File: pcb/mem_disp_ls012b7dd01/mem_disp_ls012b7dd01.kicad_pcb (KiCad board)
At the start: 2 copper layers, 11 x 41.5 mm, 4 parts, among them J1 Pin Header, J2 FCP Connector

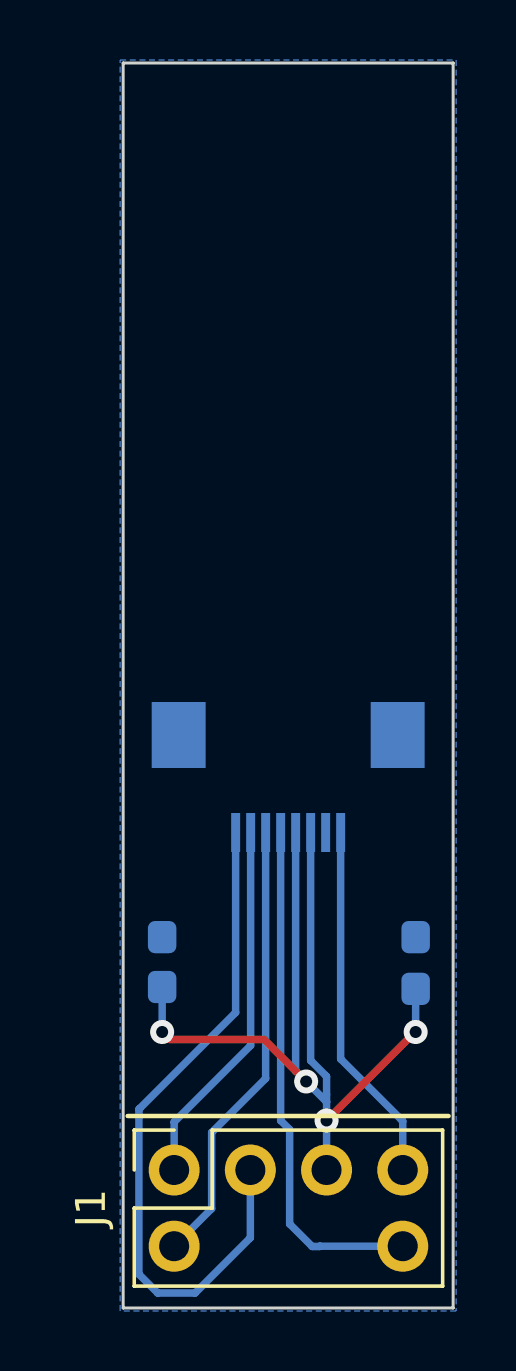
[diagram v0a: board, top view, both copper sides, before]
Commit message: Fixed capacitor mix up
VDD pin was connected to DISP capacitor and DISP capacitor was connected to VDD.

From an electrical perspective it didn’t matter though.
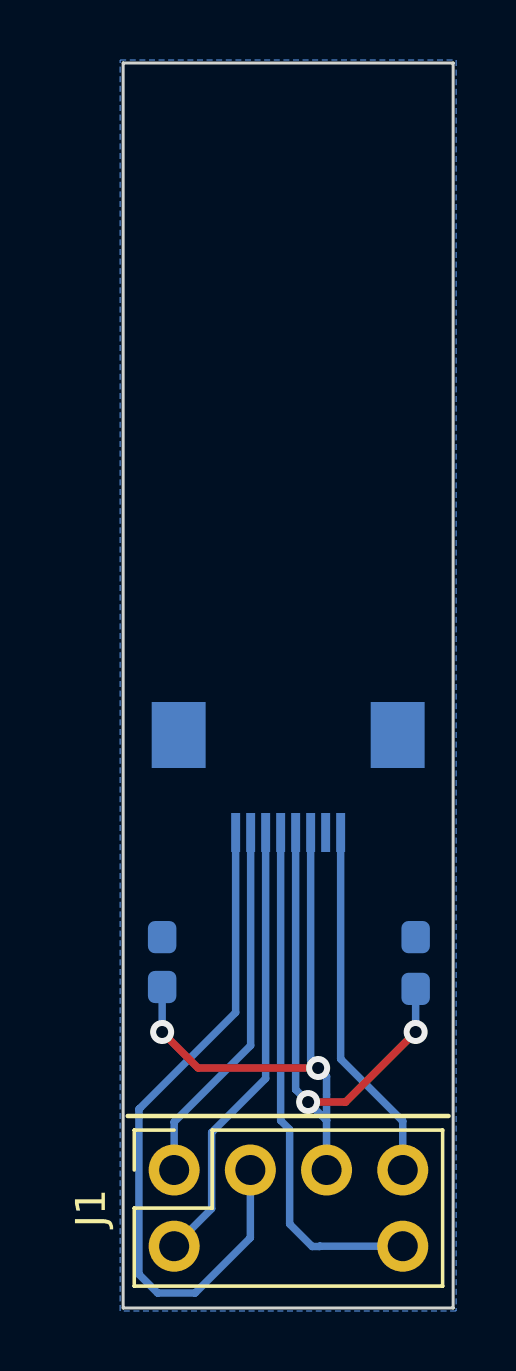
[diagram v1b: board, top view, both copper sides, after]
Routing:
- net VDD: track 33.5 -> 34.7 mm
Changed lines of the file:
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@@
     (style (thickness 0.15) (arrow_length 1.27) (text_position_mode 0) (extension_height 0.58642) (extension_offset 0.5) keep_text_aligned)
   )
-  (segment (start 51.55 83.05) (end 54.7 83.05) (width 0.25) (layer "F.Cu") (net 1))
-  (segment (start 51.3 82.8) (end 51.55 83.05) (width 0.25) (layer "F.Cu") (net 1))
-  (segment (start 54.7 83.05) (end 56.1 84.45) (width 0.25) (layer "F.Cu") (net 1))
-  (segment (start 56.78 85.75) (end 59.73 82.8) (width 0.25) (layer "F.Cu") (net 1))
-  (segment (start 59.73 82.8) (end 59.75 82.8) (width 0.25) (layer "F.Cu") (net 1))
+  (segment (start 56.165 85.135) (end 57.415 85.135) (width 0.25) (layer "F.Cu") (net 1))
+  (segment (start 52.5 84) (end 51.3 82.8) (width 0.25) (layer "F.Cu") (net 1))
+  (segment (start 57.415 85.135) (end 59.75 82.8) (width 0.25) (layer "F.Cu") (net 1))
+  (segment (start 56.5 84) (end 52.5 84) (width 0.25) (layer "F.Cu") (net 1))
+  (via (at 56.165 85.135) (size 0.8) (drill 0.4) (layers "F.Cu" "B.Cu") (net 1))
+  (via (at 51.3 82.8) (size 0.8) (drill 0.4) (layers "F.Cu" "B.Cu") (net 1))
   (via (at 59.75 82.8) (size 0.8) (drill 0.4) (layers "F.Cu" "B.Cu") (net 1))
-  (via (at 56.1 84.45) (size 0.8) (drill 0.4) (layers "F.Cu" "B.Cu") (net 1))
-  (via (at 51.3 82.8) (size 0.8) (drill 0.4) (layers "F.Cu" "B.Cu") (net 1))
-  (via (at 56.78 85.75) (size 0.8) (drill 0.4) (layers "F.Cu" "B.Cu") (net 1))
-  (segment (start 55.75 76.15) (end 55.75 84.1) (width 0.25) (layer "B.Cu") (net 1))
+  (via (at 56.5 84) (size 0.8) (drill 0.4) (layers "F.Cu" "B.Cu") (net 1))
   (segment (start 56.78 84.88) (end 56.78 84.28) (width 0.25) (layer "B.Cu") (net 1))
   (segment (start 56.78 85.75) (end 56.78 85.13) (width 0.25) (layer "B.Cu") (net 1))
-  (segment (start 55.75 84.1) (end 56.1 84.45) (width 0.25) (layer "B.Cu") (net 1))
   (segment (start 51.3 82.8) (end 51.3 81.3) (width 0.25) (layer "B.Cu") (net 1))
-  (segment (start 56.78 84.28) (end 56.25 83.75) (width 0.25) (layer "B.Cu") (net 1))
-  (segment (start 56.1 84.45) (end 56.78 85.13) (width 0.25) (layer "B.Cu") (net 1))
+  (segment (start 55.75 76.15) (end 55.75 84.72) (width 0.25) (layer "B.Cu") (net 1))
+  (segment (start 55.75 84.72) (end 56.165 85.135) (width 0.25) (layer "B.Cu") (net 1))
+  (segment (start 56.78 84.28) (end 56.5 84) (width 0.25) (layer "B.Cu") (net 1))
+  (segment (start 56.165 85.135) (end 56.78 85.75) (width 0.25) (layer "B.Cu") (net 1))
   (segment (start 56.78 85.75) (end 56.78 87.4) (width 0.25) (layer "B.Cu") (net 1))
   (segment (start 56.25 83.75) (end 56.25 76.15) (width 0.25) (layer "B.Cu") (net 1))
   (segment (start 59.75 82.8) (end 59.75 81.3625) (width 0.25) (layer "B.Cu") (net 1))
+  (segment (start 56.5 84) (end 56.25 83.75) (width 0.25) (layer "B.Cu") (net 1))
   (segment (start 56.78 85.13) (end 56.78 84.88) (width 0.25) (layer "B.Cu") (net 1))
   (segment (start 59.32 85.77) (end 59.275 85.725) (width 0.25) (layer "B.Cu") (net 2))

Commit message: Fixed C1 capacity from 20uF to 2.0uF
The 2017 datasheet seems to show that a 20uF capacitor is requiered, but in reality 2.0uF is the correct value.

The font in the datasheet is squished, which causes the "." to merge with the
"2".

Older datasheets also show a value of 2.0.
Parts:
- C2: value 20uF -> 2.0uF
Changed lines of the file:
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@@
       (effects (font (size 1 1) (thickness 0.15)) (justify mirror))
     )
-    (fp_text value "20uF" (at 0 -1.43 90) (layer "B.Fab") hide
+    (fp_text value "2.0uF" (at 0 -1.43 90) (layer "B.Fab") hide
       (effects (font (size 1 1) (thickness 0.15)) (justify mirror))
     )

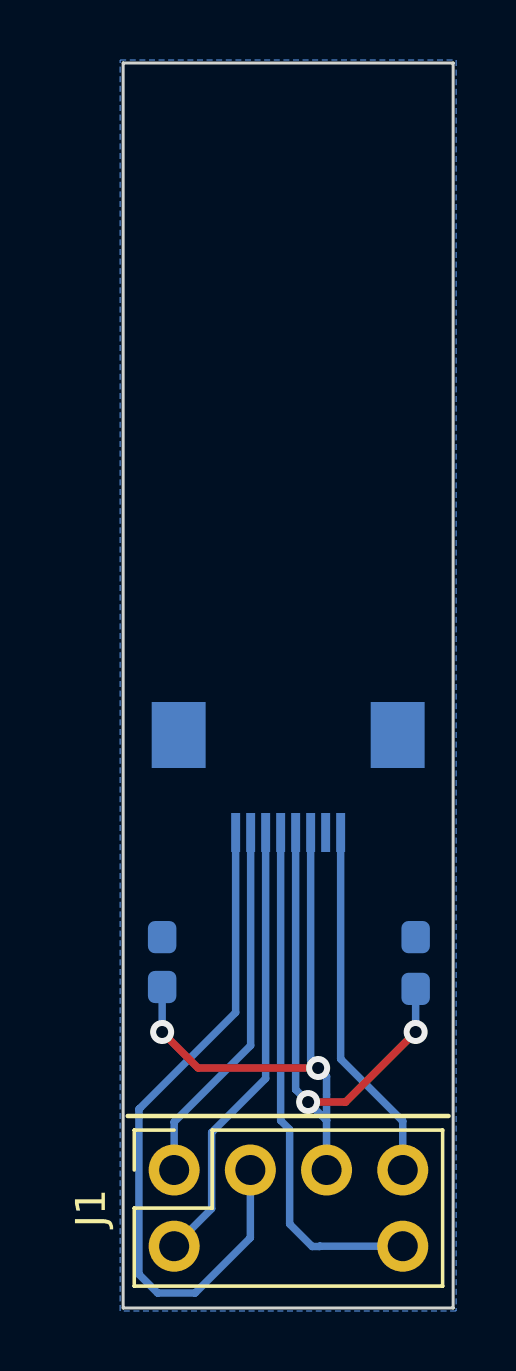
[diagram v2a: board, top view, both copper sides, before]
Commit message: Removed DISP C1 capacitor
The datasheet calls for a 560pF capacitor (C1) connected to DISP, but since we are connecting DISP to VDD, which already has a large capacitor, that's not necessary.
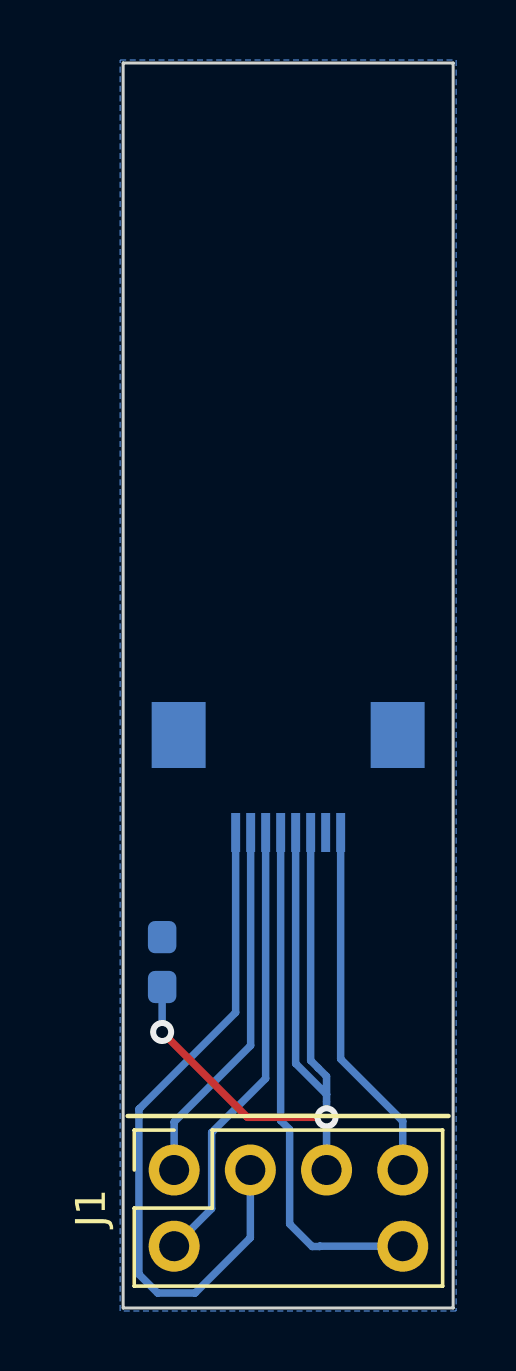
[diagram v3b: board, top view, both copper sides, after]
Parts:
- removed C1: 560pF/680pF, Capacitor_SMD:C_0603_1608Metric_Pad1.08x0.95mm_HandSolder
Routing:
- net VDD: track 34.7 -> 28.8 mm, vias 4 -> 2
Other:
- board text added: "Shap Memory Disp. (LS012B7DD01) Breakout Board v0.2"
- board text removed: "Shap Memory Disp. (LS012B7DD01) Breakout Board v0.1"
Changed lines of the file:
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@@
-    )
-  )
-  (footprint "Capacitor_SMD:C_0603_1608Metric_Pad1.08x0.95mm_HandSolder" (layer "B.Cu")
-    (at 59.75 80.5 90)
-    (descr "Capacitor SMD 0603 (1608 Metric), square (rectangular) end terminal, IPC_7351 nominal with elongated pad for handsoldering. (Body size source: IPC-SM-782 page 76, https://www.pcb-3d.com/wordpress/wp-content/uploads/ipc-sm-782a_amendment_1_and_2.pdf), generated with kicad-footprint-generator")
-    (tags "capacitor handsolder")
-    (property "Sheetfile" "mem_disp_ls012b7dd01.kicad_sch")
-    (property "Sheetname" "")
-    (attr smd)
-    (fp_text reference "C1" (at 2.35 0 180) (layer "B.SilkS")
-      (effects (font (size 1 1) (thickness 0.15)) (justify mirror))
-    )
-    (fp_text value "560pF/680pF" (at -2.85 3.1 90) (layer "B.Fab") hide
-      (effects (font (size 1 1) (thickness 0.15)) (justify mirror))
-    )
-    (fp_text user "${REFERENCE}" (at 0 0 90) (layer "B.Fab")
-      (effects (font (size 0.4 0.4) (thickness 0.06)) (justify mirror))
-    )
-    (fp_line (start -0.146267 0.51) (end 0.146267 0.51) (layer "B.SilkS") (width 0.12))
-    (fp_line (start -0.146267 -0.51) (end 0.146267 -0.51) (layer "B.SilkS") (width 0.12))
-    (fp_line (start -1.65 0.73) (end 1.65 0.73) (layer "B.CrtYd") (width 0.05))
-    (fp_line (start 1.65 0.73) (end 1.65 -0.73) (layer "B.CrtYd") (width 0.05))
-    (fp_line (start -1.65 -0.73) (end -1.65 0.73) (layer "B.CrtYd") (width 0.05))
-    (fp_line (start 1.65 -0.73) (end -1.65 -0.73) (layer "B.CrtYd") (width 0.05))
-    (fp_line (start 0.8 0.4) (end 0.8 -0.4) (layer "B.Fab") (width 0.1))
-    (fp_line (start -0.8 -0.4) (end -0.8 0.4) (layer "B.Fab") (width 0.1))
-    (fp_line (start 0.8 -0.4) (end -0.8 -0.4) (layer "B.Fab") (width 0.1))
-    (fp_line (start -0.8 0.4) (end 0.8 0.4) (layer "B.Fab") (width 0.1))
-    (pad "1" smd roundrect (at -0.8625 0 90) (size 1.075 0.95) (layers "B.Cu" "B.Paste" "B.Mask") (roundrect_rratio 0.25)
-      (net 1 "VDD") (pintype "passive"))
-    (pad "2" smd roundrect (at 0.8625 0 90) (size 1.075 0.95) (layers "B.Cu" "B.Paste" "B.Mask") (roundrect_rratio 0.25)
-      (net 2 "GND") (pintype "passive"))
-    (model "${KICAD6_3DMODEL_DIR}/Capacitor_SMD.3dshapes/C_0603_1608Metric.wrl"
-      (offset (xyz 0 0 0))
-      (scale (xyz 1 1 1))
-      (rotate (xyz 0 0 0))
     )
   )
@@
   (gr_line (start 61 92) (end 61 50.5) (layer "Edge.Cuts") (width 0.1))
   (gr_line (start 50 92) (end 61 92) (layer "Edge.Cuts") (width 0.1))
-  (gr_text "Shap Memory Disp.\n(LS012B7DD01)\nBreakout Board v0.1" (at 55.6 53.4) (layer "B.SilkS")
+  (gr_text "Shap Memory Disp.\n(LS012B7DD01)\nBreakout Board v0.2" (at 55.6 53.4) (layer "B.SilkS")
     (effects (font (size 0.5 0.5) (thickness 0.125)) (justify mirror))
   )
@@
     (style (thickness 0.15) (arrow_length 1.27) (text_position_mode 0) (extension_height 0.58642) (extension_offset 0.5) keep_text_aligned)
   )
-  (segment (start 56.165 85.135) (end 57.415 85.135) (width 0.25) (layer "F.Cu") (net 1))
-  (segment (start 52.5 84) (end 51.3 82.8) (width 0.25) (layer "F.Cu") (net 1))
-  (segment (start 57.415 85.135) (end 59.75 82.8) (width 0.25) (layer "F.Cu") (net 1))
-  (segment (start 56.5 84) (end 52.5 84) (width 0.25) (layer "F.Cu") (net 1))
-  (via (at 56.165 85.135) (size 0.8) (drill 0.4) (layers "F.Cu" "B.Cu") (net 1))
+  (segment (start 54.145 85.645) (end 51.3 82.8) (width 0.25) (layer "F.Cu") (net 1))
+  (segment (start 56.78 85.645) (end 54.145 85.645) (width 0.25) (layer "F.Cu") (net 1))
   (via (at 51.3 82.8) (size 0.8) (drill 0.4) (layers "F.Cu" "B.Cu") (net 1))
-  (via (at 59.75 82.8) (size 0.8) (drill 0.4) (layers "F.Cu" "B.Cu") (net 1))
-  (via (at 56.5 84) (size 0.8) (drill 0.4) (layers "F.Cu" "B.Cu") (net 1))
+  (via (at 56.78 85.645) (size 0.8) (drill 0.4) (layers "F.Cu" "B.Cu") (net 1))
+  (segment (start 56.78 85.645) (end 56.78 85.13) (width 0.25) (layer "B.Cu") (net 1))
+  (segment (start 55.75 83.85) (end 56.78 84.88) (width 0.25) (layer "B.Cu") (net 1))
   (segment (start 56.78 84.88) (end 56.78 84.28) (width 0.25) (layer "B.Cu") (net 1))
-  (segment (start 56.78 85.75) (end 56.78 85.13) (width 0.25) (layer "B.Cu") (net 1))
+  (segment (start 56.78 85.75) (end 56.78 85.645) (width 0.25) (layer "B.Cu") (net 1))
   (segment (start 51.3 82.8) (end 51.3 81.3) (width 0.25) (layer "B.Cu") (net 1))
-  (segment (start 55.75 76.15) (end 55.75 84.72) (width 0.25) (layer "B.Cu") (net 1))
-  (segment (start 55.75 84.72) (end 56.165 85.135) (width 0.25) (layer "B.Cu") (net 1))
+  (segment (start 55.75 76.15) (end 55.75 83.85) (width 0.25) (layer "B.Cu") (net 1))
   (segment (start 56.78 84.28) (end 56.5 84) (width 0.25) (layer "B.Cu") (net 1))
-  (segment (start 56.165 85.135) (end 56.78 85.75) (width 0.25) (layer "B.Cu") (net 1))
   (segment (start 56.78 85.75) (end 56.78 87.4) (width 0.25) (layer "B.Cu") (net 1))
   (segment (start 56.25 83.75) (end 56.25 76.15) (width 0.25) (layer "B.Cu") (net 1))
-  (segment (start 59.75 82.8) (end 59.75 81.3625) (width 0.25) (layer "B.Cu") (net 1))
   (segment (start 56.5 84) (end 56.25 83.75) (width 0.25) (layer "B.Cu") (net 1))
   (segment (start 56.78 85.13) (end 56.78 84.88) (width 0.25) (layer "B.Cu") (net 1))
